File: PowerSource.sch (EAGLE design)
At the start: 11 parts

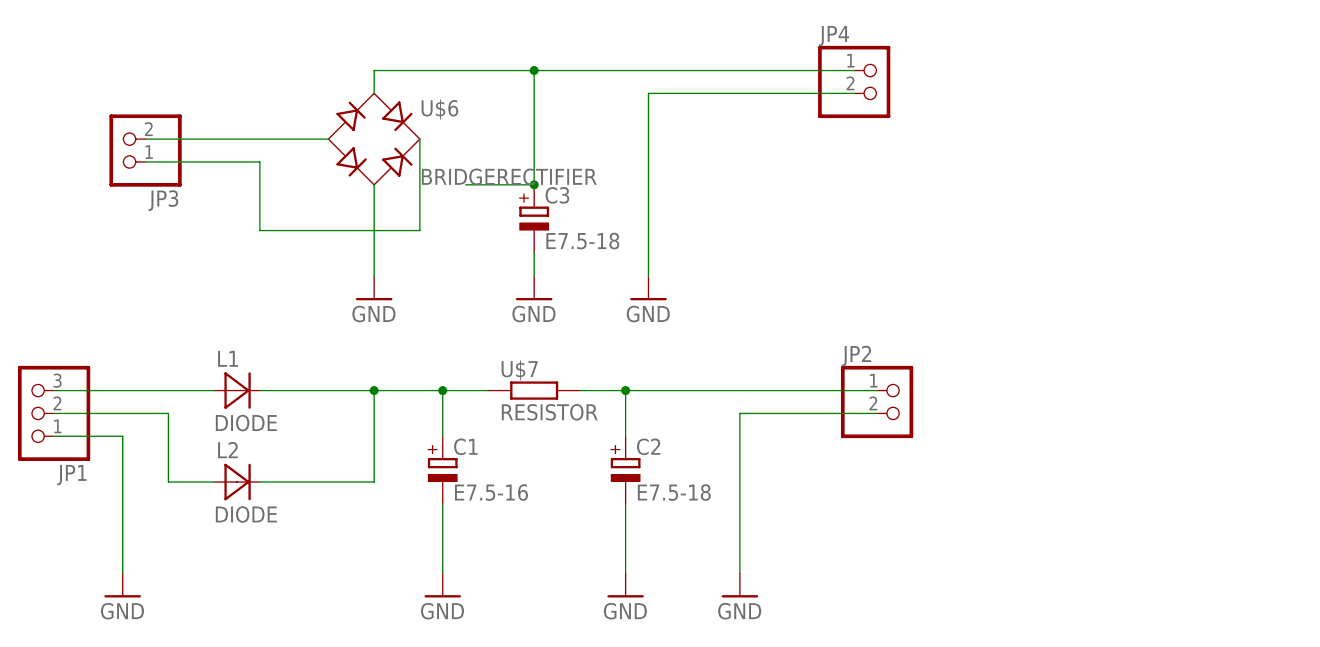
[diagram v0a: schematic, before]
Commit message: [fix]電源回路を手直し
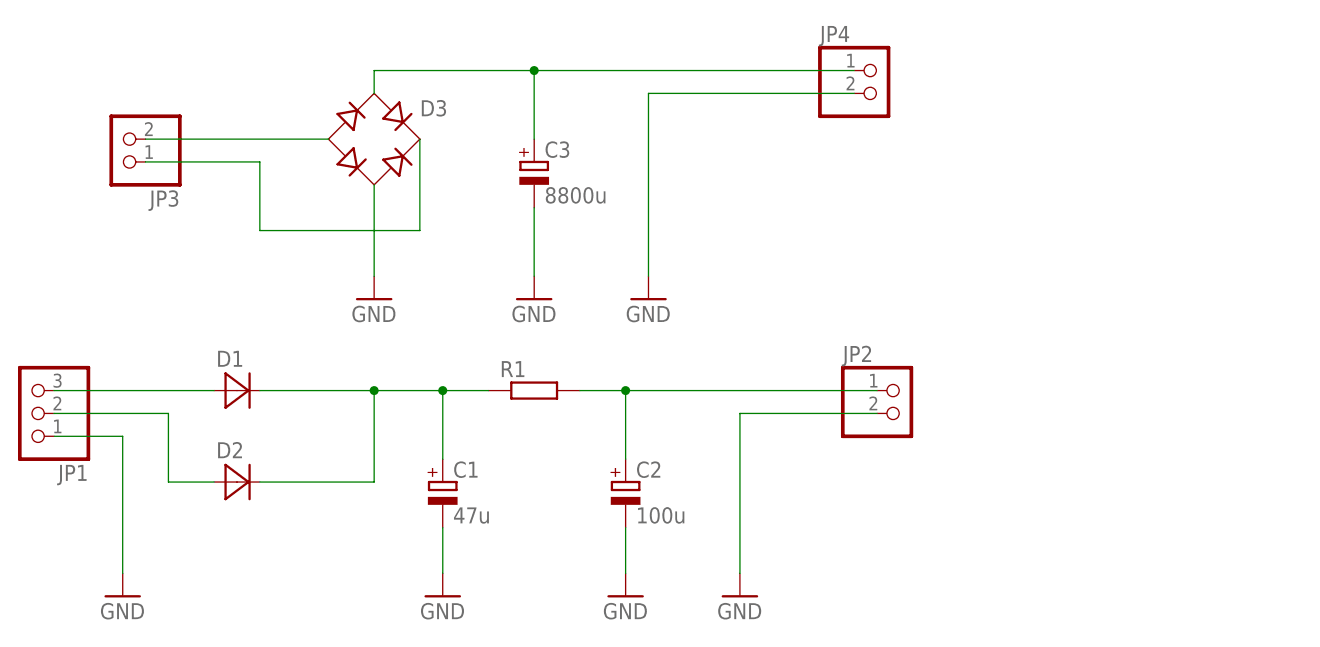
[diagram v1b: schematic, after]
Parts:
- removed U$7: RESISTOR, VacuumTube:RESISTOR
- added R1: (no value), VacuumTube:RESISTOR2
- C1: value E7.5-16 -> 47u
- C2: value E7.5-18 -> 100u
- C3: value E7.5-18 -> 8800u
- D1, D2: value DIODE -> (none)
- D3: value BRIDGERECTIFIER -> (none)
- renumbered L1 to D1, L2 to D2, U$6 to D3
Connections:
- net N$14: now also R1.2; no longer U$7.2
- net N$15: now also R1.1; no longer U$7.1
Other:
- moved on the sheet: C1, C2, C3

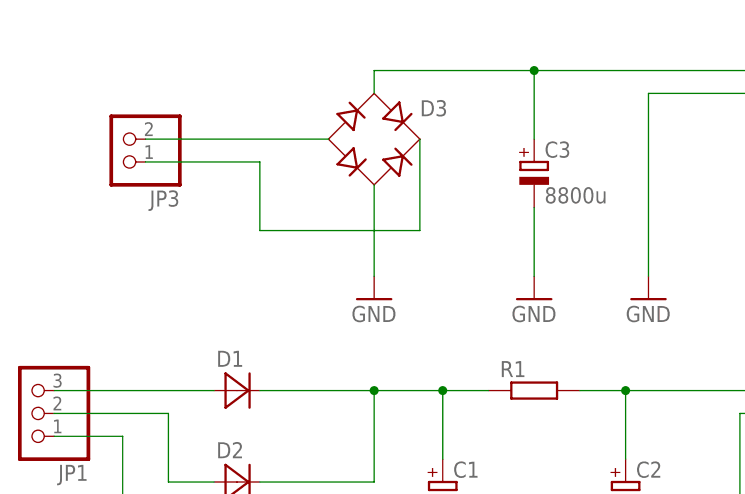
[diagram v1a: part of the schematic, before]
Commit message: [fix]電源の重大な欠陥
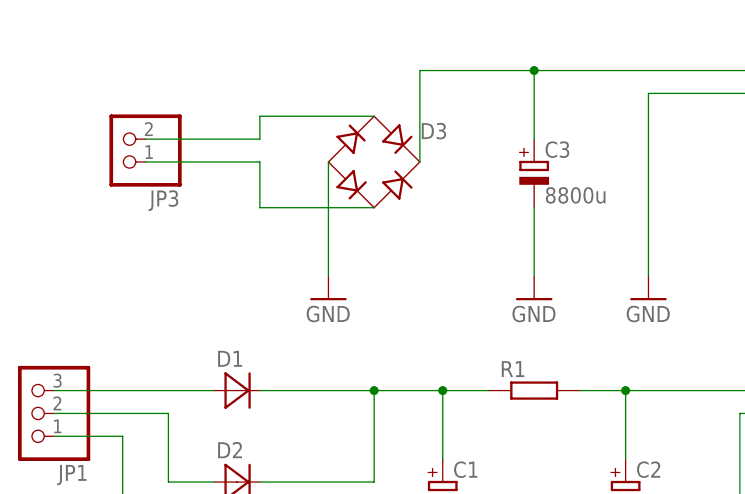
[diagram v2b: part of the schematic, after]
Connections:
- net GND: now also D3.-; no longer D3.AC2
- net N$3: now also D3.AC1; no longer D3.-
- net N$4: now also D3.AC2; no longer D3.+
- net N$7: now also D3.+; no longer D3.AC1
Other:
- moved on the sheet: D3
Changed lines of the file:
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@@
 <attribute name="VALUE" x="5.08" y="68.58" size="1.778" layer="96"/>
 </instance>
-<instance part="GND3" gate="1" x="-33.02" y="104.14" smashed="yes">
-<attribute name="VALUE" x="-35.56" y="101.6" size="1.778" layer="96"/>
+<instance part="GND3" gate="1" x="-38.1" y="104.14" smashed="yes">
+<attribute name="VALUE" x="-40.64" y="101.6" size="1.778" layer="96"/>
 </instance>
 <instance part="GND4" gate="1" x="-15.24" y="104.14" smashed="yes">
@@
 <attribute name="VALUE" x="-50.8254" y="79.3242" size="1.778" layer="96"/>
 </instance>
-<instance part="D3" gate="G$1" x="-33.02" y="121.92" smashed="yes">
-<attribute name="VALUE" x="-27.94" y="116.84" size="1.778" layer="96"/>
-<attribute name="NAME" x="-27.94" y="124.46" size="1.778" layer="95"/>
+<instance part="D3" gate="G$1" x="-33.02" y="119.38" smashed="yes">
+<attribute name="VALUE" x="-27.94" y="114.3" size="1.778" layer="96"/>
+<attribute name="NAME" x="-27.94" y="121.92" size="1.778" layer="95"/>
 </instance>
 <instance part="C1" gate="G$1" x="-25.4" y="83.82" smashed="yes">
@@
 </segment>
 <segment>
-<wire x1="-33.02" y1="116.84" x2="-33.02" y2="106.68" width="0.1524" layer="91"/>
-<pinref part="GND3" gate="1" pin="GND"/>
-<pinref part="D3" gate="G$1" pin="AC2"/>
-</segment>
-<segment>
 <pinref part="GND2" gate="1" pin="GND"/>
 <wire x1="7.62" y1="91.44" x2="7.62" y2="73.66" width="0.1524" layer="91"/>
@@
 <pinref part="GND4" gate="1" pin="GND"/>
 <wire x1="-15.24" y1="114.3" x2="-15.24" y2="106.68" width="0.1524" layer="91"/>
+</segment>
+<segment>
+<pinref part="D3" gate="G$1" pin="-"/>
+<pinref part="GND3" gate="1" pin="GND"/>
+<wire x1="-38.1" y1="119.38" x2="-38.1" y2="106.68" width="0.1524" layer="91"/>
 </segment>
 </net>
@@
 </segment>
 </net>
-<net name="N$4" class="0">
-<segment>
-<wire x1="-27.94" y1="111.76" x2="-45.72" y2="111.76" width="0.1524" layer="91"/>
-<wire x1="-45.72" y1="119.38" x2="-45.72" y2="111.76" width="0.1524" layer="91"/>
-<pinref part="JP3" gate="G$1" pin="1"/>
-<wire x1="-58.42" y1="119.38" x2="-45.72" y2="119.38" width="0.1524" layer="91"/>
-<wire x1="-27.94" y1="121.92" x2="-27.94" y2="111.76" width="0.1524" layer="91"/>
-<pinref part="D3" gate="G$1" pin="+"/>
-</segment>
-</net>
 <net name="N$7" class="0">
 <segment>
-<wire x1="-33.02" y1="127" x2="-33.02" y2="129.54" width="0.1524" layer="91"/>
-<wire x1="-33.02" y1="129.54" x2="-15.24" y2="129.54" width="0.1524" layer="91"/>
 <pinref part="JP4" gate="G$1" pin="1"/>
-<pinref part="D3" gate="G$1" pin="AC1"/>
 <pinref part="C3" gate="G$1" pin="+"/>
 <wire x1="-15.24" y1="129.54" x2="20.32" y2="129.54" width="0.1524" layer="91"/>
 <wire x1="-15.24" y1="121.92" x2="-15.24" y2="129.54" width="0.1524" layer="91"/>
+<pinref part="D3" gate="G$1" pin="+"/>
+<wire x1="-27.94" y1="119.38" x2="-27.94" y2="129.54" width="0.1524" layer="91"/>
+<wire x1="-27.94" y1="129.54" x2="-15.24" y2="129.54" width="0.1524" layer="91"/>
 <junction x="-15.24" y="129.54"/>
 </segment>
@@
 <segment>
 <pinref part="JP3" gate="G$1" pin="2"/>
-<wire x1="-58.42" y1="121.92" x2="-38.1" y2="121.92" width="0.1524" layer="91"/>
-<pinref part="D3" gate="G$1" pin="-"/>
+<wire x1="-58.42" y1="121.92" x2="-45.72" y2="121.92" width="0.1524" layer="91"/>
+<pinref part="D3" gate="G$1" pin="AC1"/>
+<wire x1="-45.72" y1="121.92" x2="-45.72" y2="124.46" width="0.1524" layer="91"/>
+<wire x1="-45.72" y1="124.46" x2="-33.02" y2="124.46" width="0.1524" layer="91"/>
 </segment>
 </net>
+<net name="N$4" class="0">
+<segment>
+<pinref part="D3" gate="G$1" pin="AC2"/>
+<wire x1="-33.02" y1="114.3" x2="-45.72" y2="114.3" width="0.1524" layer="91"/>
+<wire x1="-45.72" y1="114.3" x2="-45.72" y2="119.38" width="0.1524" layer="91"/>
+<pinref part="JP3" gate="G$1" pin="1"/>
+<wire x1="-45.72" y1="119.38" x2="-58.42" y2="119.38" width="0.1524" layer="91"/>
+</segment>
+</net>

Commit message: [fix]電源の直し
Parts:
- C1: value 47u -> 100u
- C2: value 100u -> 47u
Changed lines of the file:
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@@
 <part name="D2" library="VacuumTube" library_urn="urn:adsk.eagle:library:8044196" deviceset="DIODE" device="" package3d_urn="urn:adsk.eagle:package:8399791/1"/>
 <part name="D3" library="VacuumTube" library_urn="urn:adsk.eagle:library:8044196" deviceset="BRIDGERECTIFIER" device="" package3d_urn="urn:adsk.eagle:package:8399794/1"/>
-<part name="C1" library="VacuumTube" library_urn="urn:adsk.eagle:library:8044196" deviceset="E7.5-16" device="" package3d_urn="urn:adsk.eagle:package:8399792/3" value="47u"/>
-<part name="C2" library="VacuumTube" library_urn="urn:adsk.eagle:library:8044196" deviceset="E7.5-18" device="" package3d_urn="urn:adsk.eagle:package:8399793/3" value="100u"/>
+<part name="C1" library="VacuumTube" library_urn="urn:adsk.eagle:library:8044196" deviceset="E7.5-16" device="" package3d_urn="urn:adsk.eagle:package:8399792/3" value="100u"/>
+<part name="C2" library="VacuumTube" library_urn="urn:adsk.eagle:library:8044196" deviceset="E7.5-18" device="" package3d_urn="urn:adsk.eagle:package:8399793/3" value="47u"/>
 <part name="C3" library="VacuumTube" library_urn="urn:adsk.eagle:library:8044196" deviceset="E7.5-18" device="" package3d_urn="urn:adsk.eagle:package:8399793/3" value="8800u"/>
 <part name="R1" library="VacuumTube" library_urn="urn:adsk.eagle:library:8044196" deviceset="RESISTOR2" device="" package3d_urn="urn:adsk.eagle:package:8969348/1"/>

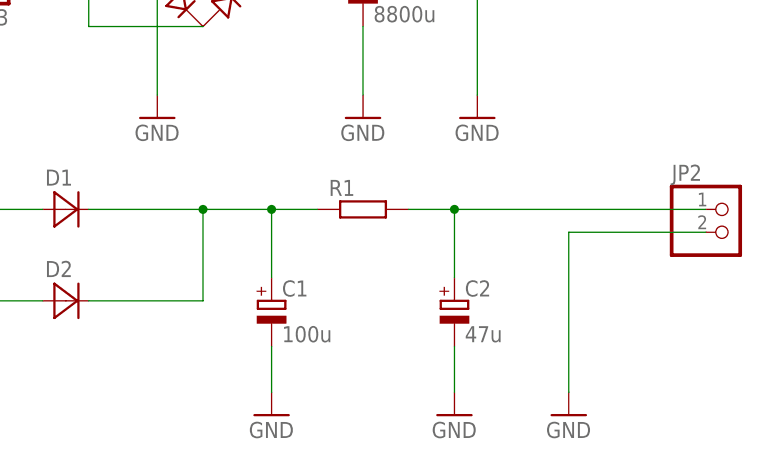
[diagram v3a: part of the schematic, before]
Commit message: [add]powerのpdfを作成
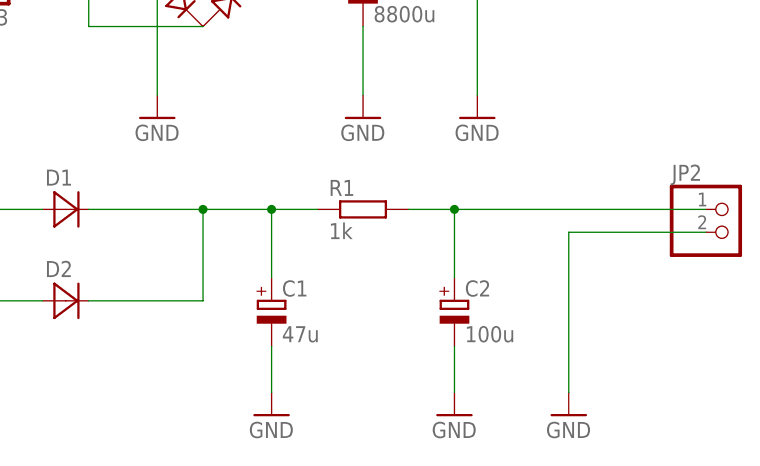
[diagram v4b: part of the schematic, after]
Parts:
- C1: value 100u -> 47u
- C2: value 47u -> 100u
- R1: value (none) -> 1k
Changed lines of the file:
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@@
 <part name="D2" library="VacuumTube" library_urn="urn:adsk.eagle:library:8044196" deviceset="DIODE" device="" package3d_urn="urn:adsk.eagle:package:8399791/1"/>
 <part name="D3" library="VacuumTube" library_urn="urn:adsk.eagle:library:8044196" deviceset="BRIDGERECTIFIER" device="" package3d_urn="urn:adsk.eagle:package:8399794/1"/>
-<part name="C1" library="VacuumTube" library_urn="urn:adsk.eagle:library:8044196" deviceset="E7.5-16" device="" package3d_urn="urn:adsk.eagle:package:8399792/3" value="100u"/>
-<part name="C2" library="VacuumTube" library_urn="urn:adsk.eagle:library:8044196" deviceset="E7.5-18" device="" package3d_urn="urn:adsk.eagle:package:8399793/3" value="47u"/>
+<part name="C1" library="VacuumTube" library_urn="urn:adsk.eagle:library:8044196" deviceset="E7.5-16" device="" package3d_urn="urn:adsk.eagle:package:8399792/3" value="47u"/>
+<part name="C2" library="VacuumTube" library_urn="urn:adsk.eagle:library:8044196" deviceset="E7.5-18" device="" package3d_urn="urn:adsk.eagle:package:8399793/3" value="100u"/>
 <part name="C3" library="VacuumTube" library_urn="urn:adsk.eagle:library:8044196" deviceset="E7.5-18" device="" package3d_urn="urn:adsk.eagle:package:8399793/3" value="8800u"/>
-<part name="R1" library="VacuumTube" library_urn="urn:adsk.eagle:library:8044196" deviceset="RESISTOR2" device="" package3d_urn="urn:adsk.eagle:package:8969348/1"/>
+<part name="R1" library="VacuumTube" library_urn="urn:adsk.eagle:library:8044196" deviceset="RESISTOR2" device="" package3d_urn="urn:adsk.eagle:package:8969348/1" value="1k"/>
 </parts>
 <sheets>

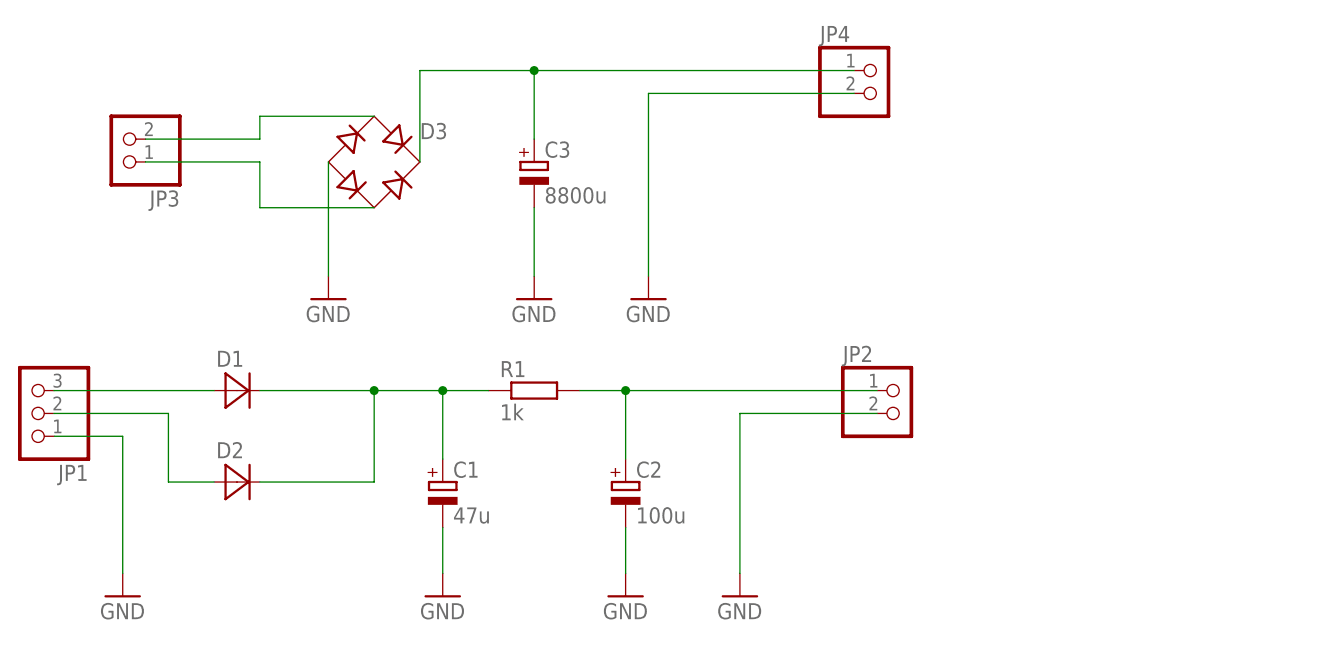
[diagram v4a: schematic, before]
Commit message: [fix]ヒーター電源を二つ使うことにした
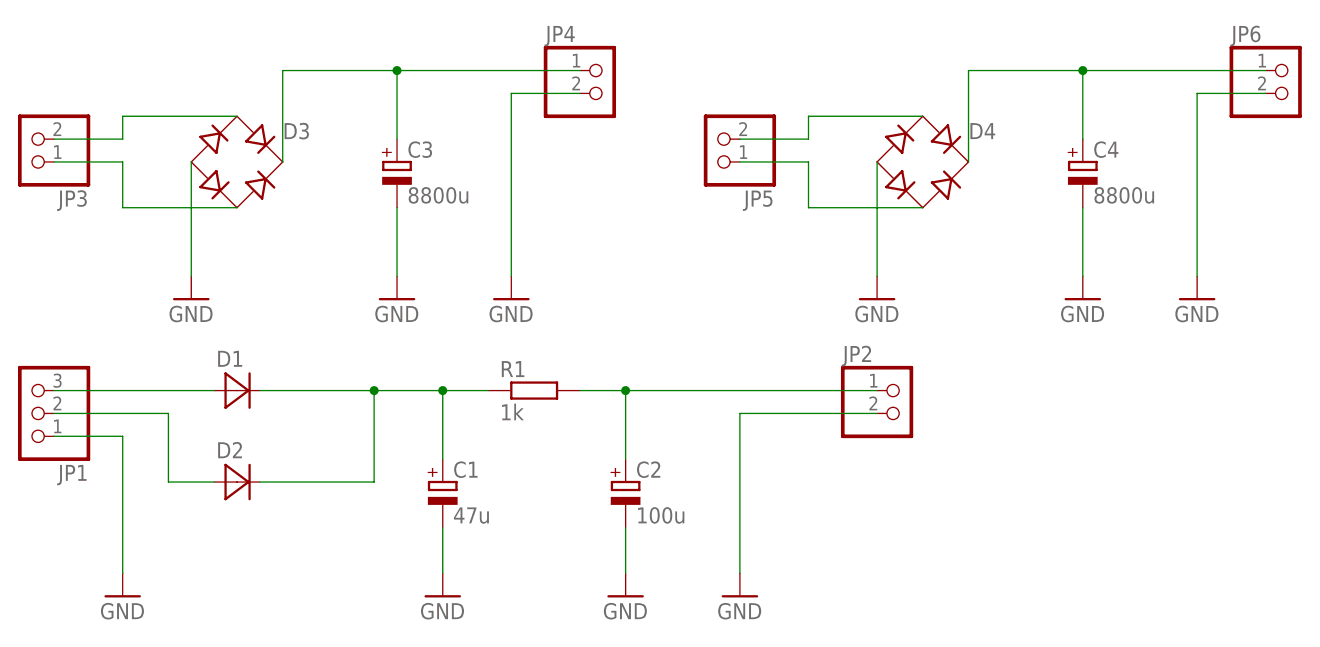
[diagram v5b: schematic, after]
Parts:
- added C4: 8800u, VacuumTube:E7.5-18
- added D4: (no value), VacuumTube:BRIDGERECTIFIER
- added JP5, JP6: (no value), VacuumTube:PINHD-1X2
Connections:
- new net N$5: C4.+, D4.+, JP6.1
- new net N$6: D4.AC1, JP5.2
- new net N$8: D4.AC2, JP5.1
- net GND: now also C4.-, D4.-, JP6.2
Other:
- moved on the sheet: C3, D3, JP3, JP4
